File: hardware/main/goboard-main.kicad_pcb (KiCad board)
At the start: 2 copper layers, 304.7 x 114.2 mm, 198 parts, among them J1 USB_C_Receptacle_USB2.0, J2 Conn_02x05_Top_Bottom, J3 Conn_01x01, J4 Conn_01x05, Q1 SSM3J338R, Q10 SSM3J338R, Q2 BCP53, Q3 SSM3J338R, Q4 BC817, Q5 SSM3J338R, Q6 BC807, Q7 BC817, Q8 SSM3J338R, Q9 SSM3J338R, SW1 Esc, SW10 a, SW11 SW_Push, SW12 Fn, SW13 F2, SW14 2, SW15 w, SW16 s, SW17 z, SW18 Tux, SW19 F3, SW2 F1, SW20 3, SW21 e, SW22 d, SW23 c, SW24 Alt, SW25 F4, SW26 4, SW27 r, SW28 f, SW29 v, SW3 tilde, SW30 SW_DP3T, SW31 F5, SW32 5, SW33 t, SW34 g, SW35 b, SW36 F6, SW37 6, SW38 y, SW39 h, SW4 Tab, SW40 n, SW41 F7, SW42 7, SW43 u, SW44 j, SW45 m, SW46 Space, SW47 F8, SW48 8, SW49 i, SW5 Caps Lock, SW50 k, SW51 comma, SW52 F9, SW53 9, SW54 o, SW55 l, SW56 dot, SW57 F10, SW58 0, SW59 p, SW6 Shift, SW60 semicolon, SW61 slash, SW62 Alt Gr, SW63 F11, SW64 minus, SW65 sq br open, SW66 apostrophe, SW67 Menu, SW68 F12, SW69 equal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

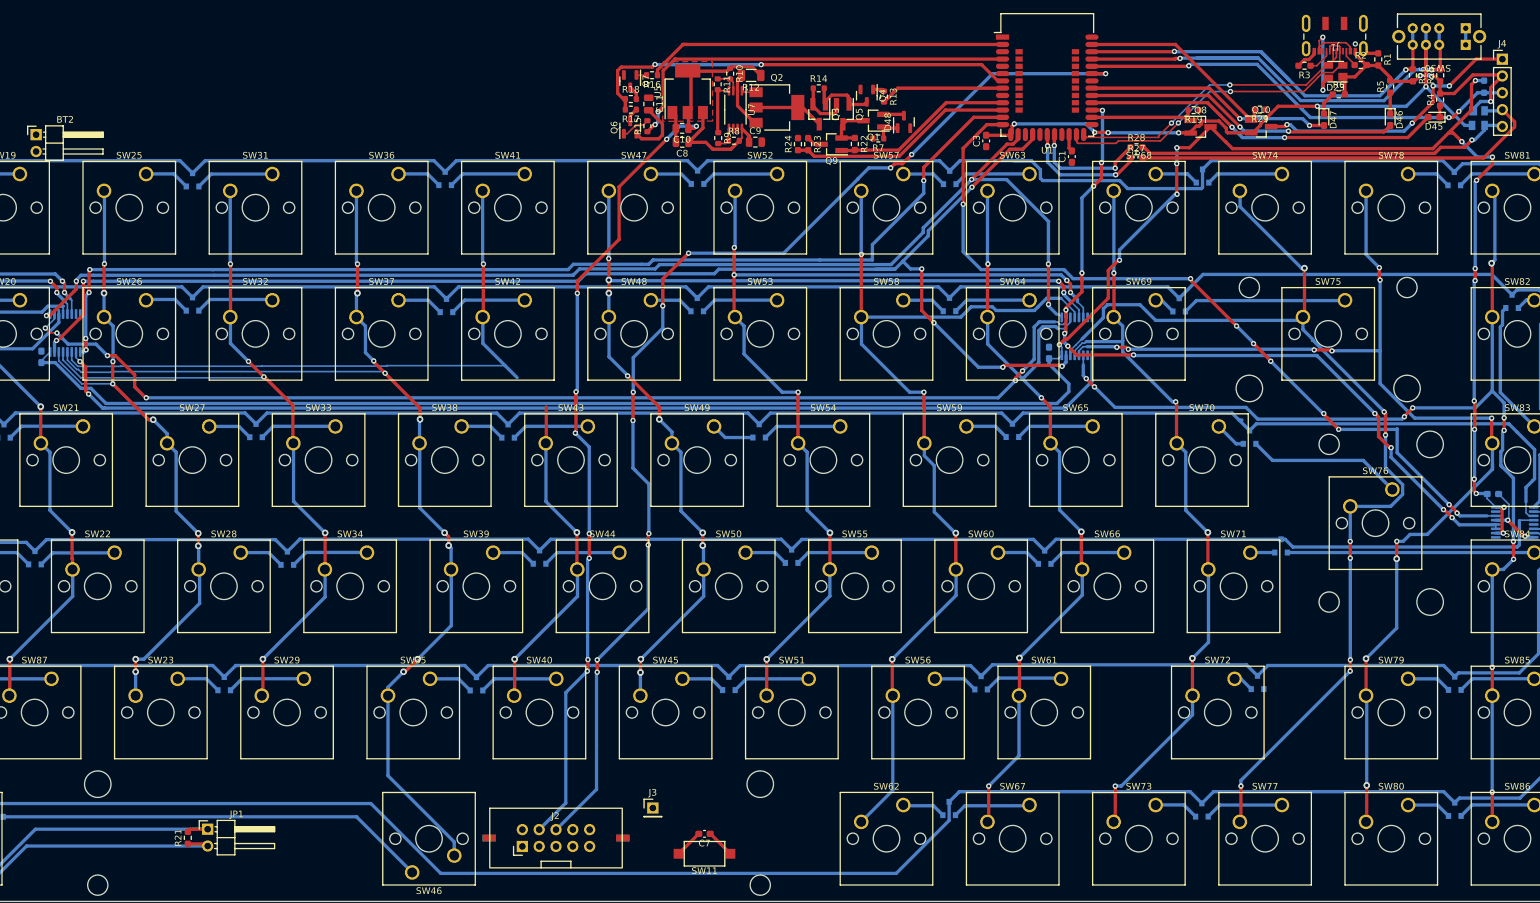
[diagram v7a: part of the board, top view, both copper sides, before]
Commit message: Re-add USB voltage sense circuit
Due to firmware limitations the USB voltage cannot be used directly for
waking up the microcontroller.
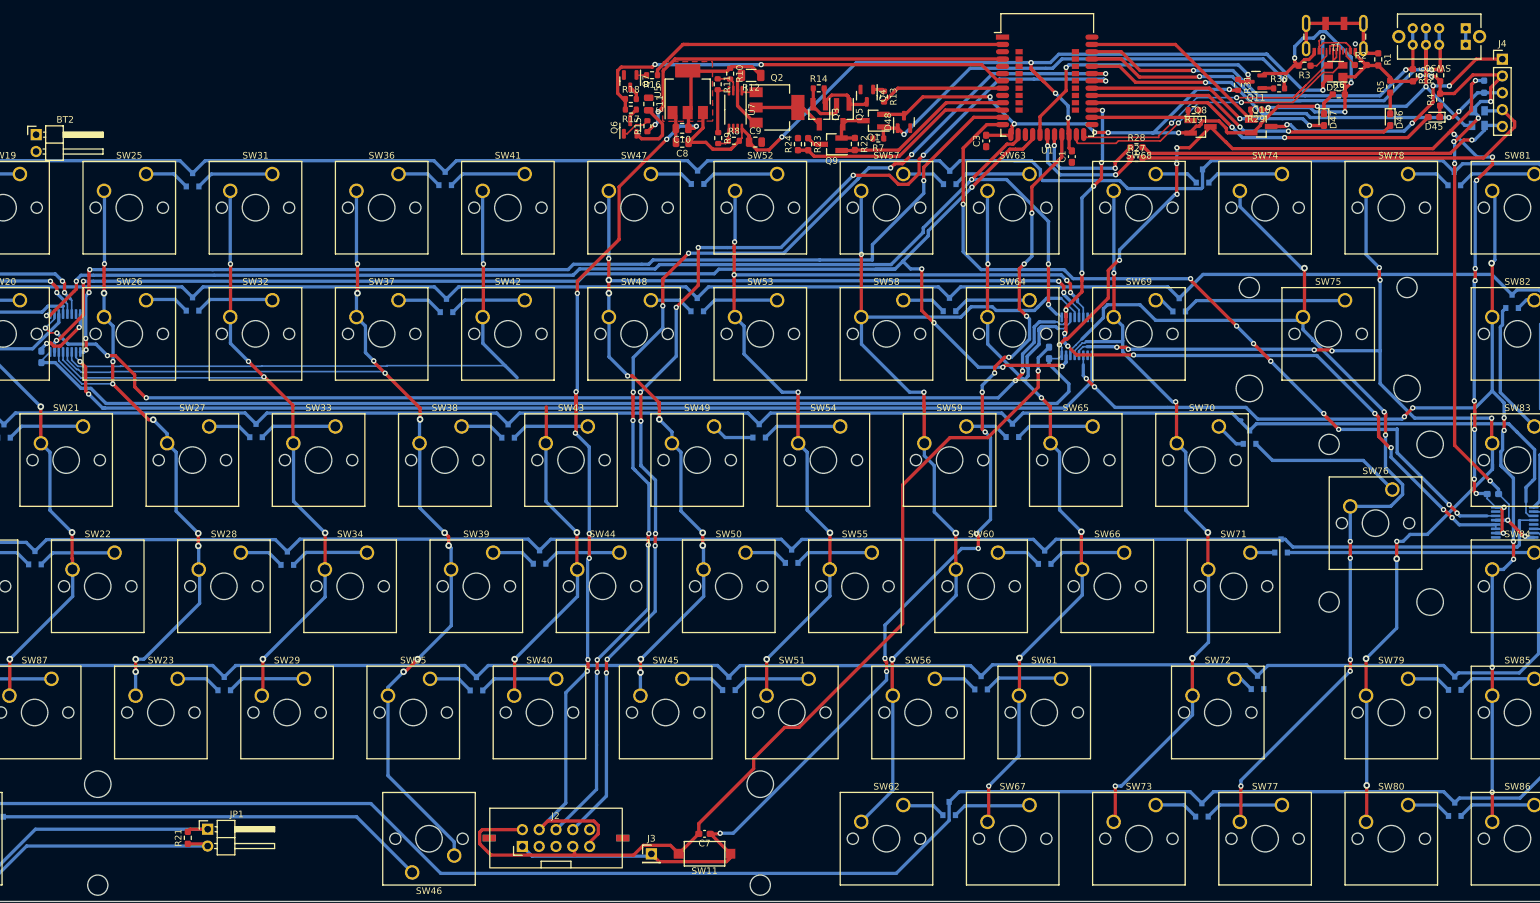
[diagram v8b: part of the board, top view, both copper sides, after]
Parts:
- added Q11: BC817, Package_TO_SOT_SMD:SOT-23, F.Cu at (293.7, 62.3)
- added R30: 4.7K, Resistor_SMD:R_0603_1608Metric, F.Cu at (297.2, 63.3)
- added R31: 10K, Resistor_SMD:R_0603_1608Metric, F.Cu at (291.0, 62.7)
- moved J3 6.93 mm to (202.5, 178.8)
- moved R29 0.55 mm to (293.8, 66.5)
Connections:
- U1 pad 18: unconnected-(U1-Pad18) -> /MCU/~USB_CONN
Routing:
- net GND: track 76.3 -> 332.2 mm, vias 5 -> 16
- net /SWDCLK: track 0.00 -> 174.2 mm, vias 0 -> 11
- net /RESET: track 4.28 -> 172.4 mm, vias 0 -> 12
- net +5V: track 40.1 -> 151.6 mm, vias 2 -> 6
- net +3V3: track 147.7 -> 227.3 mm, vias 9 -> 11
- net /MCU/~USB_CONN: track 0.00 -> 43.1 mm, vias 0 -> 2
- net /VCC_SW: track 100.2 -> 135.6 mm, vias 6 -> 8
- net Net-(J1-PadS1): track 2.54 -> 18.8 mm
- net /switch_bt_2: track 65.2 -> 59.1 mm
- net /USB_D+: track 46.8 -> 49.6 mm
- net /switch_bt_1: track 72.8 -> 70.1 mm
- net Net-(SW61-Pad2): track 121.8 -> 123.9 mm
- net Net-(Q11-Pad1): track 0.00 -> 1.75 mm
- net Net-(SW45-Pad2): track 161.6 -> 162.7 mm
